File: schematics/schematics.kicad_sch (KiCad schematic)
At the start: 32 parts, among them J1 USB_C_Receptacle_USB2.0_14P, J2 BAT, SW1 MS1, SW2 MS2, SW3 MS3, SW4 RST, SW5 BOOT, U1 ESP32-C3-WROOM-02, U2 MPU-6050, U3 AMS1117-3.3, U4 LTC4054ES5-4.2

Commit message: initial electronics
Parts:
- removed C1: 22u, symbol Device:C_Polarized
- removed SW1: MS1, symbol Switch:SW_Push
- removed SW2: MS2, symbol Switch:SW_Push
- removed SW3: MS3, symbol Switch:SW_Push
- removed U2: MPU-6050, Sensor_Motion:InvenSense_QFN-24_4x4mm_P0.5mm, symbol Sensor_Motion:MPU-6050
- removed U3: AMS1117-3.3, Package_TO_SOT_SMD:SOT-223-3_TabPin2, symbol Regulator_Linear:AMS1117-3.3
- added C1, C10: 1u, Capacitor_SMD:C_0805_2012Metric, symbol Device:C
- added C11, C12: 10n, Capacitor_SMD:C_0603_1608Metric, symbol Device:C
- added C13, C14: 100n, Capacitor_SMD:C_0603_1608Metric, symbol Device:C
- added J3: BT1, TerminalBlock_Phoenix:TerminalBlock_Phoenix_MPT-0,5-2-2.54_1x02_P2.54mm_Horizontal, symbol Connector:Screw_Terminal_01x02
- added J4: BT2, TerminalBlock_Phoenix:TerminalBlock_Phoenix_MPT-0,5-2-2.54_1x02_P2.54mm_Horizontal, symbol Connector:Screw_Terminal_01x02
- added J5: BT3, TerminalBlock_Phoenix:TerminalBlock_Phoenix_MPT-0,5-2-2.54_1x02_P2.54mm_Horizontal, symbol Connector:Screw_Terminal_01x02
- added R10, R11: 10k, Resistor_SMD:R_0603_1608Metric, symbol Device:R
- added R12, R13, R14: 1k, Resistor_SMD:R_0603_1608Metric, symbol Device:R
- added SW1: SW_SPDT, Button_Switch_SMD:SW_SPDT_PCM12, symbol Switch:SW_SPDT
- added U2, U3: SPX3819M5-L-3-3, Package_TO_SOT_SMD:SOT-23-5, symbol Regulator_Linear:SPX3819M5-L-3-3
- added U5: TVS1400DRV, Package_SON:WSON-6-1EP_2x2mm_P0.65mm_EP1x1.6mm, symbol Power_Protection:TVS1400DRV
- added U6: ~, Package_LGA:Bosch_LGA-14_3x2.5mm_P0.5mm, symbol BMI270:BMI270
- C2, C5, C6, C7, C8: value 0.1u -> 100n; footprint (none) -> Capacitor_SMD:C_0603_1608Metric
- C3: value 10n -> 100n; footprint (none) -> Capacitor_SMD:C_0603_1608Metric
- C4: value 2.2n -> 100n; footprint (none) -> Capacitor_SMD:C_0603_1608Metric
- C9: value 0.1u -> 1u; footprint (none) -> Capacitor_SMD:C_0805_2012Metric
- D1, D2: footprint (none) -> LED_THT:LED_D1.8mm_W1.8mm_H2.4mm_Horizontal_O1.27mm_Z1.6mm
- J1: footprint (none) -> Connector_USB:USB_C_Receptacle_GCT_USB4110
- J2: footprint (none) -> Connector_JST:JST_PH_B2B-PH-K_1x02_P2.00mm_Vertical
- R1, R2, R3, R4, R5, R6, R7, R9: value 10k -> 1k; footprint (none) -> Resistor_SMD:R_0603_1608Metric
- R8: value 10k -> 330; footprint (none) -> Resistor_SMD:R_0603_1608Metric
- R_PROG1: renamed from R_PROG; value 10k -> 2k; footprint (none) -> Resistor_SMD:R_0603_1608Metric
- SW4, SW5: footprint (none) -> Button_Switch_SMD:SW_Push_1P1T_NO_CK_KMR2
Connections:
- net +3V3: now also C2.1, C1.1, C10.1, J3.2 (Pin_2), J4.2 (Pin_2), J5.2 (Pin_2), R10.1, R11.1, U2.5 (OUT), U3.5 (OUT), U6.12 (CSB), U6.14 (SDx), U6.5 (VDDI0), U6.8 (VDD)
- net +5V: now also C9.1, D1.2 (A), C13.1, U2.1 (IN), U2.3 (EN), U5.4 (IN), U5.5 (IN), U5.6 (IN); no longer R8.1
- net GND: now also R5.2, R7.2, C1.2, C10.2, C11.2, C12.2, C13.2, C14.2, R12.2, U2.2 (GND), U3.2 (GND), U5.1 (GND), U5.2 (GND), U5.3 (GND), U5.7 (GND), U6.6 (GNDI0), U6.7 (GND); no longer D1.1 (K)
- net MS1: now also U1.10 (IO10)
- net MS2: now also U1.11 (IO20/RXD), R13.2; no longer R5.2
- net MS3: now also C4.1, U1.12 (IO21/TXD), R14.2; no longer C9.1, R7.2
- net SDA: now also U1.15 (IO3), R11.2, U6.1 (SDO)
- net at R5.1: now also J4.1 (Pin_1), R13.1
- net at R6.1: now also J3.1 (Pin_1), R12.1
- net at J2.1 (Pin_1), U4.3 (BAT): now also SW1.2 (B)
- net at R7.1: now also J5.1 (Pin_1), R14.1
- net SCL: now reaches U1.16 (IO2)
- net SCL: now also R10.2, U6.13 (SCx)
- new net: C14.1, SW1.1 (A), U3.1 (IN), U3.3 (EN)
- new net: R8.1, U4.1 (~{CHRG})
- new net: C11.1, U2.4 (BP)
- new net: C12.1, U3.4 (BP)
- new net: D1.1 (K), R8.2
- no-connect marks 7 -> 14
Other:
- moved on the sheet: C2, C3, C5, C6, C7, C8, D1, D2, J1, J2, R1, R2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

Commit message: completed electronics, ordered parts
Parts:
- removed C1, C10, C9: 1u, Capacitor_SMD:C_0805_2012Metric, symbol Device:C
- added C10, C15, C9: 1u, Capacitor_SMD:C_0805_2012Metric, symbol Device:C_Polarized
- SW1: footprint Button_Switch_SMD:SW_SPDT_PCM12 -> Button_Switch_THT:SW_Slide_SPDT_Angled_CK_OS102011MA1Q
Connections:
- net +3V3: now also C10.1, C9.1
- net +5V: now also C15.1
- net GND: now also J2.1 (Pin_1), C10.2, C15.2, C9.2; no longer J2.2 (Pin_2)
- net at SW1.2 (B), U4.3 (BAT): now also J2.2 (Pin_2); no longer J2.1 (Pin_1)

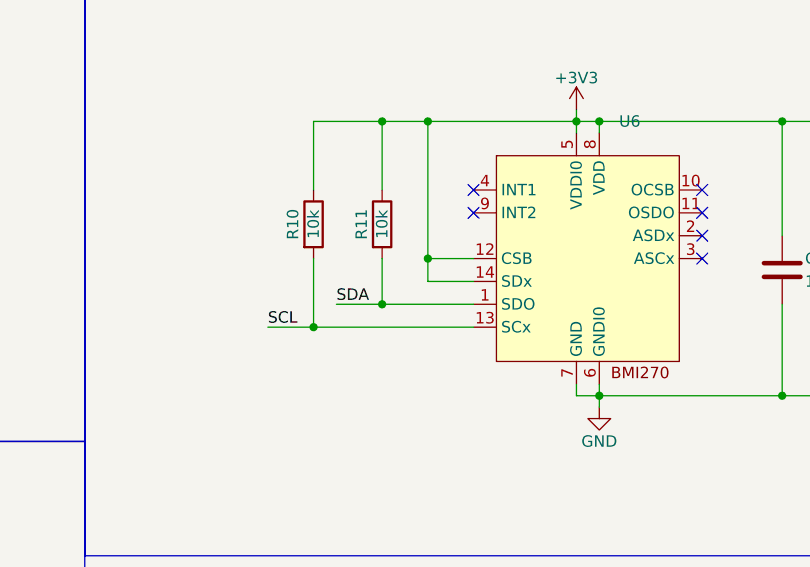
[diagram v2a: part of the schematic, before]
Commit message: fix i2c pins
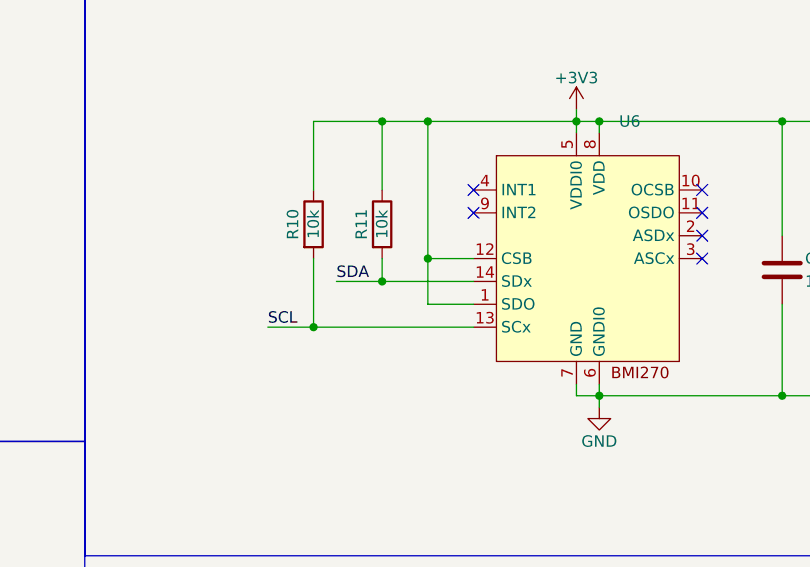
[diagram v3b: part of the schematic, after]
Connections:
- net +3V3: now also U6.1 (SDO); no longer U6.14 (SDx)
- net SDA: now also U6.14 (SDx); no longer U6.1 (SDO)
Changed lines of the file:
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@@
+	)
+	(junction
+		(at 114.3 139.7)
+		(diameter 0)
+		(color 0 0 0 0)
+	)
+	(junction
+		(at 200.66 139.7)
+		(diameter 0)
+		(color 0 0 0 0)
+	)
+	(junction
+		(at 252.73 147.32)
+		(diameter 0)
+		(color 0 0 0 0)
+	)
+	(junction
+		(at 232.41 116.84)
+		(diameter 0)
+		(color 0 0 0 0)
+	)
+	(junction
+		(at 50.8 173.99)
+		(diameter 0)
+		(color 0 0 0 0)
+	)
+	(junction
+		(at 82.55 166.37)
+		(diameter 0)
+		(color 0 0 0 0)
+	)
+	(junction
+		(at 127 139.7)
+		(diameter 0)
+		(color 0 0 0 0)
+	)
+	(junction
+		(at 217.17 64.77)
+		(diameter 0)
+		(color 0 0 0 0)
+	)
+	(junction
+		(at 114.3 123.19)
+		(diameter 0)
+		(color 0 0 0 0)
+	)
+	(junction
+		(at 109.22 74.93)
+		(diameter 0)
+		(color 0 0 0 0)
+	)
+	(junction
+		(at 132.08 74.93)
+		(diameter 0)
+		(color 0 0 0 0)
+	)
+	(junction
+		(at 213.36 116.84)
+		(diameter 0)
+		(color 0 0 0 0)
+	)
+	(junction
+		(at 76.2 109.22)
+		(diameter 0)
+		(color 0 0 0 0)
+	)
+	(junction
+		(at 83.82 173.99)
+		(diameter 0)
+		(color 0 0 0 0)
+	)
+	(junction
+		(at 66.04 184.15)
+		(diameter 0)
+		(color 0 0 0 0)
+	)
+	(junction
+		(at 50.8 166.37)
+		(diameter 0)
+		(color 0 0 0 0)
+	)
+	(junction
+		(at 120.65 74.93)
+		(diameter 0)
+		(color 0 0 0 0)
+	)
+	(junction
+		(at 207.01 64.77)
+		(diameter 0)
+		(color 0 0 0 0)
+	)
+	(junction
+		(at 232.41 147.32)
+		(diameter 0)
+		(color 0 0 0 0)
+	)
+	(junction
+		(at 99.06 184.15)
+		(diameter 0)
+		(color 0 0 0 0)
+	)
+	(junction
+		(at 226.06 80.01)
+		(diameter 0)
+		(color 0 0 0 0)
+	)
+	(junction
+		(at 198.12 36.83)
+		(diameter 0)
+		(color 0 0 0 0)
+	)
+	(junction
+		(at 86.36 74.93)
+		(diameter 0)
+		(color 0 0 0 0)
+	)
+	(junction
+		(at 86.36 35.56)
+		(diameter 0)
+		(color 0 0 0 0)
+	)
+	(junction
+		(at 66.04 49.53)
+		(diameter 0)
+		(color 0 0 0 0)
+	)
+	(junction
+		(at 252.73 116.84)
+		(diameter 0)
+		(color 0 0 0 0)
+	)
+	(junction
+		(at 207.01 24.13)
+		(diameter 0)
+		(color 0 0 0 0)
+	)
+	(junction
+		(at 148.59 120.65)
+		(diameter 0)
+		(color 0 0 0 0)
+	)
+	(junction
+		(at 229.87 116.84)
+		(diameter 0)
+		(color 0 0 0 0)
+	)
+	(junction
+		(at 132.08 184.15)
+		(diameter 0)
+		(color 0 0 0 0)
+	)
+	(junction
+		(at 208.28 116.84)
+		(diameter 0)
+		(color 0 0 0 0)
+	)
+	(junction
+		(at 217.17 80.01)
+		(diameter 0)
+		(color 0 0 0 0)
+	)
+	(junction
+		(at 62.23 139.7)
+		(diameter 0)
+		(color 0 0 0 0)
+	)
+	(junction
+		(at 116.84 173.99)
+		(diameter 0)
+		(color 0 0 0 0)
 	)
 	(junction
@@
 	)
 	(junction
-		(at 114.3 139.7)
-		(diameter 0)
-		(color 0 0 0 0)
-	)
-	(junction
-		(at 200.66 139.7)
-		(diameter 0)
-		(color 0 0 0 0)
-	)
-	(junction
-		(at 252.73 147.32)
-		(diameter 0)
-		(color 0 0 0 0)
-	)
-	(junction
-		(at 208.28 137.16)
-		(diameter 0)
-		(color 0 0 0 0)
-	)
-	(junction
-		(at 232.41 116.84)
-		(diameter 0)
-		(color 0 0 0 0)
-	)
-	(junction
-		(at 50.8 173.99)
-		(diameter 0)
-		(color 0 0 0 0)
-	)
-	(junction
-		(at 82.55 166.37)
-		(diameter 0)
-		(color 0 0 0 0)
-	)
-	(junction
-		(at 127 139.7)
-		(diameter 0)
-		(color 0 0 0 0)
-	)
-	(junction
-		(at 217.17 64.77)
-		(diameter 0)
-		(color 0 0 0 0)
-	)
-	(junction
-		(at 114.3 123.19)
-		(diameter 0)
-		(color 0 0 0 0)
-	)
-	(junction
-		(at 109.22 74.93)
-		(diameter 0)
-		(color 0 0 0 0)
-	)
-	(junction
-		(at 132.08 74.93)
-		(diameter 0)
-		(color 0 0 0 0)
-	)
-	(junction
-		(at 213.36 116.84)
-		(diameter 0)
-		(color 0 0 0 0)
-	)
-	(junction
-		(at 76.2 109.22)
-		(diameter 0)
-		(color 0 0 0 0)
-	)
-	(junction
-		(at 83.82 173.99)
-		(diameter 0)
-		(color 0 0 0 0)
-	)
-	(junction
-		(at 66.04 184.15)
-		(diameter 0)
-		(color 0 0 0 0)
-	)
-	(junction
-		(at 50.8 166.37)
-		(diameter 0)
-		(color 0 0 0 0)
-	)
-	(junction
-		(at 120.65 74.93)
-		(diameter 0)
-		(color 0 0 0 0)
-	)
-	(junction
-		(at 207.01 64.77)
-		(diameter 0)
-		(color 0 0 0 0)
-	)
-	(junction
-		(at 232.41 147.32)
-		(diameter 0)
-		(color 0 0 0 0)
-	)
-	(junction
-		(at 99.06 184.15)
-		(diameter 0)
-		(color 0 0 0 0)
-	)
-	(junction
-		(at 226.06 80.01)
-		(diameter 0)
-		(color 0 0 0 0)
-	)
-	(junction
-		(at 198.12 36.83)
-		(diameter 0)
-		(color 0 0 0 0)
-	)
-	(junction
-		(at 86.36 74.93)
-		(diameter 0)
-		(color 0 0 0 0)
-	)
-	(junction
-		(at 86.36 35.56)
-		(diameter 0)
-		(color 0 0 0 0)
-	)
-	(junction
-		(at 66.04 49.53)
-		(diameter 0)
-		(color 0 0 0 0)
-	)
-	(junction
-		(at 252.73 116.84)
-		(diameter 0)
-		(color 0 0 0 0)
-	)
-	(junction
-		(at 207.01 24.13)
-		(diameter 0)
-		(color 0 0 0 0)
-	)
-	(junction
-		(at 148.59 120.65)
-		(diameter 0)
-		(color 0 0 0 0)
-	)
-	(junction
-		(at 229.87 116.84)
-		(diameter 0)
-		(color 0 0 0 0)
-	)
-	(junction
-		(at 132.08 184.15)
-		(diameter 0)
-		(color 0 0 0 0)
-	)
-	(junction
-		(at 208.28 116.84)
-		(diameter 0)
-		(color 0 0 0 0)
-	)
-	(junction
-		(at 217.17 80.01)
-		(diameter 0)
-		(color 0 0 0 0)
-	)
-	(junction
-		(at 62.23 139.7)
-		(diameter 0)
-		(color 0 0 0 0)
-	)
-	(junction
-		(at 116.84 173.99)
-		(diameter 0)
-		(color 0 0 0 0)
-	)
-	(junction
 		(at 207.01 80.01)
 		(diameter 0)
@@
 	(junction
 		(at 198.12 80.01)
+		(diameter 0)
+		(color 0 0 0 0)
+	)
+	(junction
+		(at 208.28 134.62)
 		(diameter 0)
 		(color 0 0 0 0)
@@
 	(wire
 		(pts
-			(xy 203.2 137.16) (xy 208.28 137.16)
+			(xy 203.2 134.62) (xy 208.28 134.62)
 		)
 		(stroke
@@
 	(wire
 		(pts
-			(xy 213.36 134.62) (xy 213.36 132.08)
-		)
-		(stroke
-			(width 0)
-			(type default)
-		)
-	)
-	(wire
-		(pts
 			(xy 207.01 24.13) (xy 207.01 54.61)
 		)
@@
 	(wire
 		(pts
+			(xy 208.28 134.62) (xy 208.28 132.08)
+		)
+		(stroke
+			(width 0)
+			(type default)
+		)
+	)
+	(wire
+		(pts
 			(xy 76.2 109.22) (xy 76.2 115.57)
 		)
@@
 	(wire
 		(pts
-			(xy 208.28 137.16) (xy 208.28 132.08)
-		)
-		(stroke
-			(width 0)
-			(type default)
-		)
-	)
-	(wire
-		(pts
 			(xy 226.06 41.91) (xy 226.06 48.26)
 		)
@@
 	(wire
 		(pts
+			(xy 213.36 137.16) (xy 213.36 132.08)
+		)
+		(stroke
+			(width 0)
+			(type default)
+		)
+	)
+	(wire
+		(pts
 			(xy 262.89 147.32) (xy 262.89 137.16)
 		)
@@
 	(wire
 		(pts
+			(xy 218.44 137.16) (xy 213.36 137.16)
+		)
+		(stroke
+			(width 0)
+			(type default)
+		)
+	)
+	(wire
+		(pts
 			(xy 53.34 119.38) (xy 53.34 123.19)
 		)
@@
 	(wire
 		(pts
-			(xy 218.44 137.16) (xy 208.28 137.16)
+			(xy 208.28 134.62) (xy 218.44 134.62)
 		)
 		(stroke
@@
 		(pts
 			(xy 231.14 49.53) (xy 238.76 49.53)
-		)
-		(stroke
-			(width 0)
-			(type default)
-		)
-	)
-	(wire
-		(pts
-			(xy 218.44 134.62) (xy 213.36 134.62)
 		)
 		(stroke
@@
 	)
 	(label "SDA"
-		(at 203.2 137.16 0)
+		(at 203.2 134.62 0)
 		(effects
 			(font
